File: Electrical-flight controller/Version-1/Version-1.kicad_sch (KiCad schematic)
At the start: 48 parts, among them J1 USB_B_Micro, J2 Conn_01x08_Socket, Q1 S8050, Q2 S8050, Q4 BSS138, SW1 SW_MEC_5G, SW2 SW_MEC_5G, U1 ESP32-WROOM-32, U2 W25Q128JVE, U3 74LS04, U4 CP2102N-Axx-xQFN28, U5 AMS1117, U6 BMP390L, U7 ICM-20948

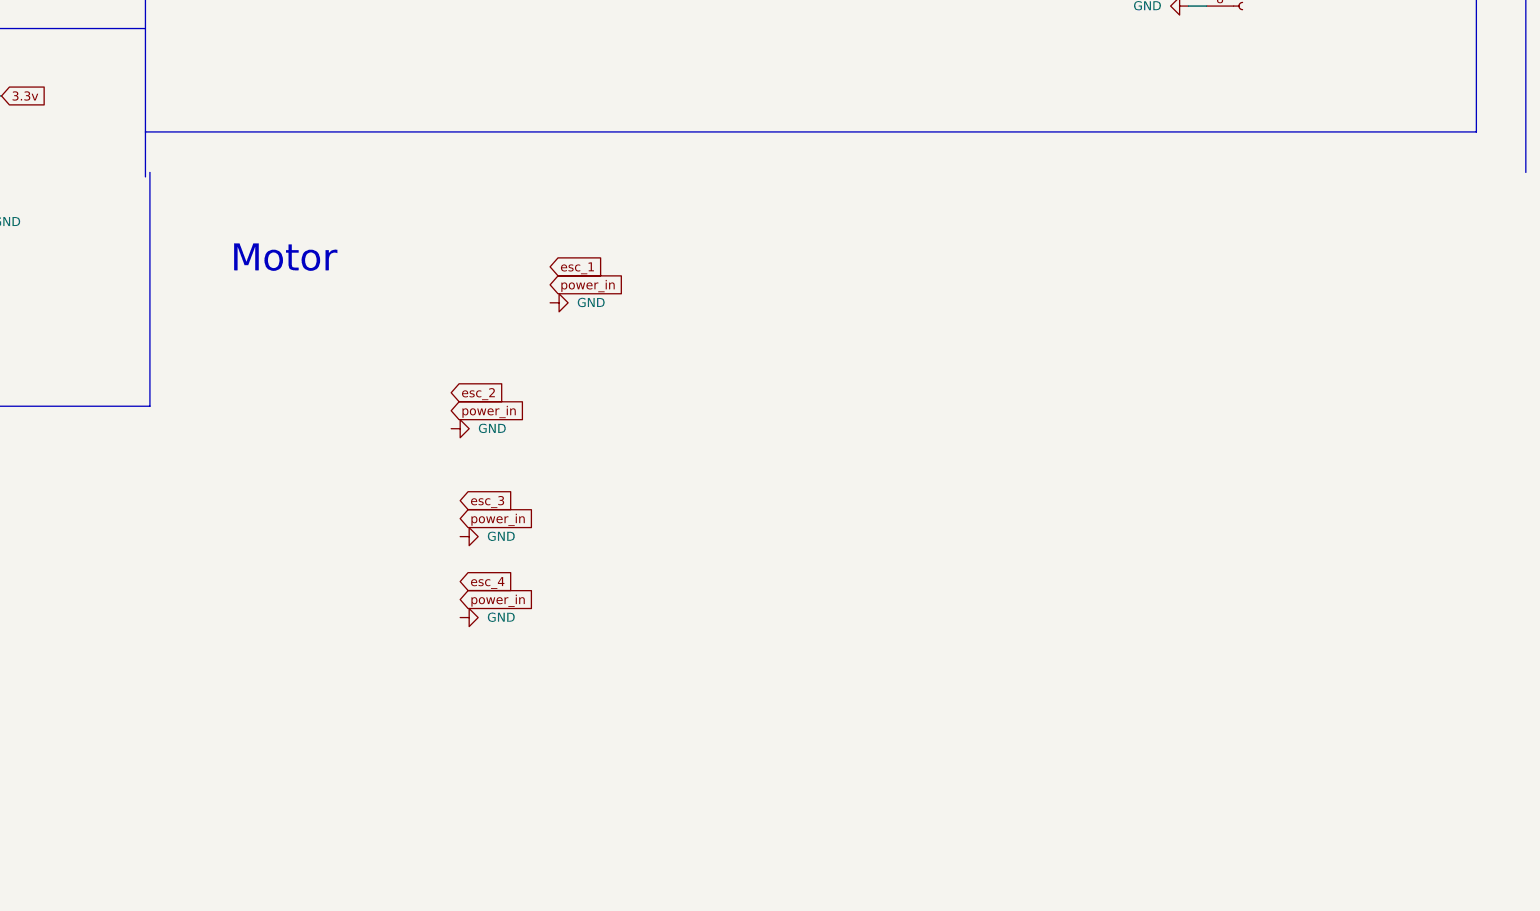
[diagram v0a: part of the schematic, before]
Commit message: added motor drivers
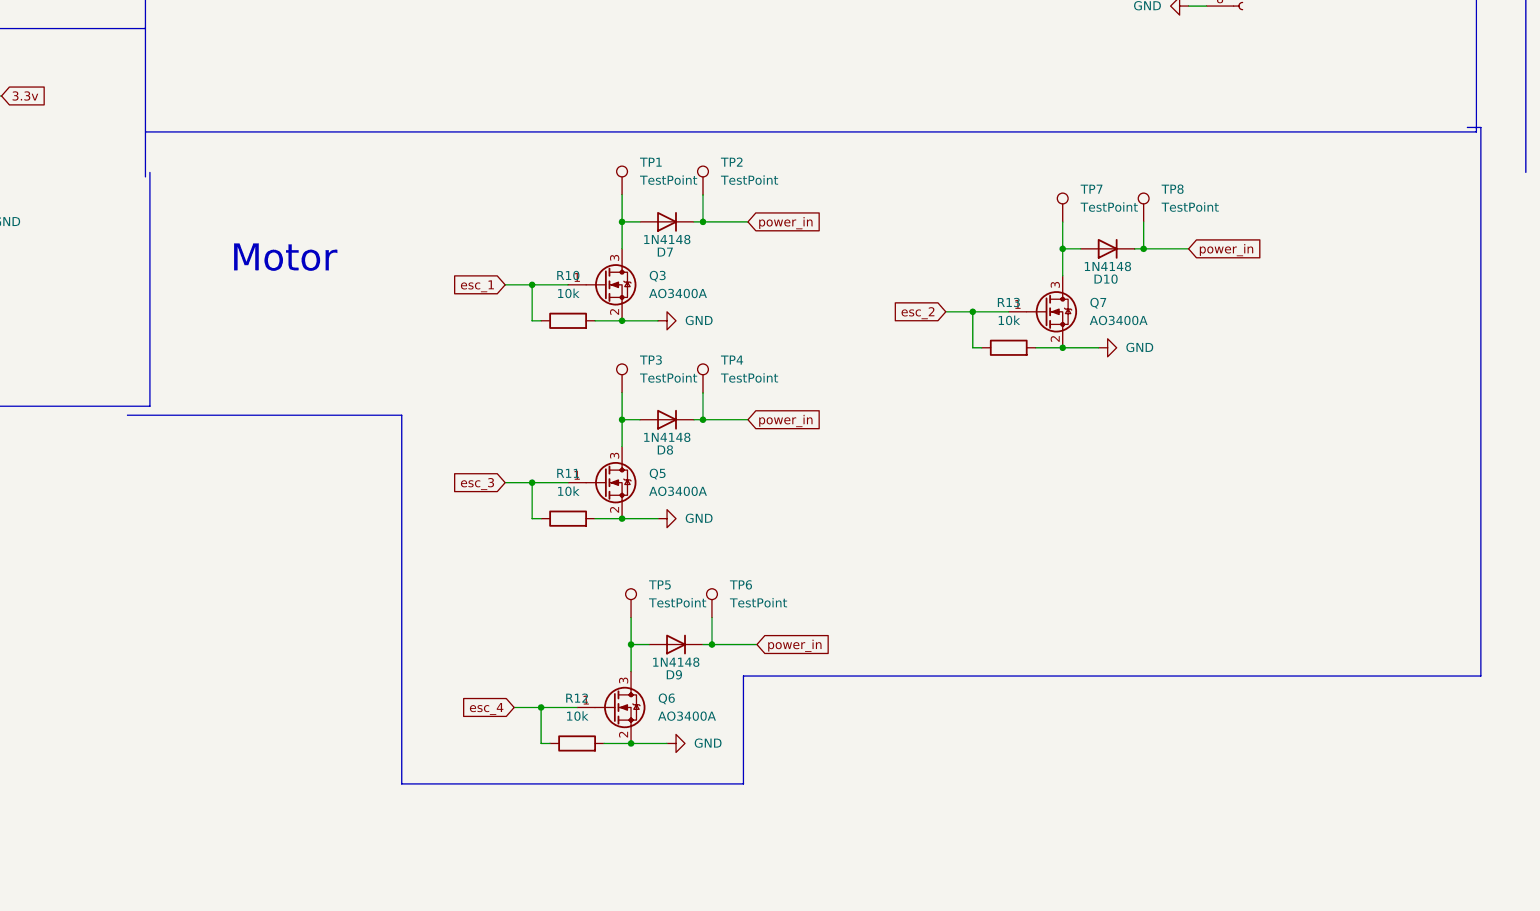
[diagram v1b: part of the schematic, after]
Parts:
- added D10, D7, D8, D9: 1N4148, Diode_THT:D_DO-35_SOD27_P7.62mm_Horizontal, symbol Diode:1N4148
- added Q3, Q5, Q6, Q7: AO3400A, Package_TO_SOT_SMD:SOT-23, symbol Transistor_FET:AO3400A
- added R10, R11, R12, R13: 10k, symbol Device:R
- added TP1, TP2, TP3, TP4, TP5, TP6, TP7, TP8: TestPoint, symbol Connector:TestPoint
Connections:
- net GND: now also Q3.2 (S), Q5.2 (S), Q6.2 (S), Q7.2 (S), R10.2, R11.2, R12.2, R13.2
- net esc_1: now also Q3.1 (G), R10.1
- net esc_2: now also Q7.1 (G), R13.1
- net esc_3: now also Q5.1 (G), R11.1
- net esc_4: now also Q6.1 (G), R12.1
- net power_in: now also D10.1 (K), D7.1 (K), D8.1 (K), D9.1 (K), TP2.1, TP4.1, TP6.1, TP8.1
- new net: D8.2 (A), Q5.3 (D), TP3.1
- new net: D9.2 (A), Q6.3 (D), TP5.1
- new net: D10.2 (A), Q7.3 (D), TP7.1
- new net: D7.2 (A), Q3.3 (D), TP1.1

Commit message: schematic complete!
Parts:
- added C10: 22uF, symbol Device:C
- added C11, C12: C, symbol Device:C
- added C23: 10uF, Capacitor_SMD:C_0603_1608Metric, symbol Device:C
- added C9: 10uF, symbol Device:C
- added D17: PMEG6020ER, Diode_SMD:Nexperia_CFP3_SOD-123W, symbol Diode:PMEG6020ER
- added J3: Conn_01x02_Socket, symbol Connector:Conn_01x02_Socket
- added L1: 1uF, symbol Device:L
- added Q8: DMG2301L, Package_TO_SOT_SMD:SOT-23, symbol Transistor_FET:DMG2301L
- added R17: 732K, symbol Device:R
- added R18: 100K, symbol Device:R
- added U8: TPS61022, Package_DFN_QFN:Texas_RWU0007A_VQFN-7_2x2mm_P0.5mm, symbol Converter_DCDC:TPS61022
- added U9: LTC4412xS6, Package_TO_SOT_SMD:TSOT-23-6, symbol Power_Management:LTC4412xS6
- R10, R11, R12, R13: value 10k -> 10K
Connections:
- net +3.3V: no longer BZ1.1 (+)
- net 3.3v: now also BZ1.1 (+)
- net 5v: now also D17.2 (A); no longer C3.1, R4.1, U5.3 (VI)
- net GND: now also C10.2, C11.2, C12.2, C23.2, C9.2, J3.2 (Pin_2), R18.2, U8.1 (GND), U9.2 (GND), U9.3 (CTL)
- net power_in: no longer D10.1 (K), D7.1 (K), D8.1 (K), D9.1 (K), TP2.1, TP4.1, TP6.1, TP8.1
- new net: R17.2, R18.1, U8.4 (FB)
- new net: Q8.1 (G), U9.5 (GATE)
- new net: L1.2, U8.2 (SW)
- new net BAT+: C9.1, J3.1 (Pin_1), L1.1, U8.5 (EN), U8.7 (VIN)
- new net BAT_IN: C10.1, C11.1, C12.1, D10.1 (K), D7.1 (K), D8.1 (K), D9.1 (K), Q8.3 (D), R17.1, TP2.1, TP4.1, TP6.1, TP8.1, U8.3 (VOUT), U9.1 (VIN)
- new net SWITCHOUT: C23.1, C3.1, D17.1 (K), Q8.2 (S), R4.1, U5.3 (VI), U9.6 (SENSE)
- no-connect marks 32 -> 33

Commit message: imported footprints and assigned them
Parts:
- removed TP1, TP2, TP3, TP4, TP5, TP6, TP7, TP8: TestPoint, symbol Connector:TestPoint
- added J4, J5, J6, J7: Conn_01x02_Socket, Connector_JST:JST_PH_B2B-PH-K_1x02_P2.00mm_Vertical, symbol Connector:Conn_01x02_Socket
- C1, C10, C2, C3, C4, C5, C6, C7, C8, C9: footprint (none) -> Capacitor_SMD:C_0603_1608Metric
- C11, C12: value C -> 22uF; footprint (none) -> Capacitor_SMD:C_0603_1608Metric
- D1: footprint (none) -> LED_SMD:LED_0201_0603Metric
- D2, D3, D4: footprint (none) -> LESD5D5.0CT1G:TVS_LESD5D5.0CT1G
- D6: footprint (none) -> ESD33v88DC:ESD33v88DC
- J1: footprint (none) -> Connector_USB:USB_Micro-B_GCT_USB3076-30-A
- J2: footprint (none) -> Connector_PinSocket_2.54mm:PinSocket_1x08_P2.54mm_Vertical
- J3: footprint (none) -> Connector_JST:JST_PH_B2B-PH-K_1x02_P2.00mm_Vertical
- L1: value 1uF -> 1uH; footprint (none) -> MLF2012A1R0KT000:INDC2012X105N
- R1, R10, R11, R12, R13, R14, R15, R16, R17, R18, R2, R3, R4, R5, R6, R7, R8, R9: footprint (none) -> Resistor_SMD:R_0402_1005Metric
- SW1, SW2: footprint (none) -> TS-1187A-B-A-B:SW_TS-1187A-B-A-B
- U3: footprint (none) -> Package_DIP:DIP-14_W7.62mm_Socket_LongPads
- U6: footprint barometer:XDCR_BMP390L.kicad_mod -> Package_LGA:ST_HLGA-10_2x2mm_P0.5mm_LayoutBorder3x2y
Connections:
- net +3.3V is gone; now on net 3.3v: J2.3 (Pin_3)
- net EP is gone; now on net GND: U2.9 (EP)
- net BAT_IN: now also J4.2 (Pin_2), J5.2 (Pin_2), J6.2 (Pin_2), J7.2 (Pin_2)
- net DI: now also U1.27 (IO16); no longer U1.13 (IO14)
- net DO: now also U1.28 (IO17); no longer U1.27 (IO16)
- net I2C-CL: now also U1.36 (IO22); no longer U1.28 (IO17)
- net IO13: now also U1.16 (IO13)
- net IO15: now also U1.23 (IO15)
- net SCK: no longer U1.16 (IO13), U2.6 (CLK)
- net USB_DN: now also U4.5 (D-)
- net USB_DP: no longer U4.5 (D-)
- net at D8.2 (A), Q5.3 (D): now also J5.1 (Pin_1)
- net at D9.2 (A), Q6.3 (D): now also J6.1 (Pin_1)
- net at D10.2 (A), Q7.3 (D): now also J7.1 (Pin_1)
- net at D7.2 (A), Q3.3 (D): now also J4.1 (Pin_1)
- new net SCK_flash: U1.13 (IO14), U2.6 (CLK)
- no-connect marks 33 -> 41
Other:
- moved on the sheet: C10, C11, C12, C9, J3, L1, R17, R18, U8

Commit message: started pcb -- all basic setups
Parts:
- removed U3: 74LS04, Package_DIP:DIP-14_W7.62mm_Socket_LongPads, symbol 74xx:74LS04
- added CR1, CR2, CR3: 1SS404_H3FT, USC_TOS:USC_TOS, symbol 1SS404:1SS404_H3FT
- U6: footprint Package_LGA:ST_HLGA-10_2x2mm_P0.5mm_LayoutBorder3x2y -> BMP390L:BMP390L; Availability In Stock -> (none); Check_prices https://www.snapeda.com/parts/BMP390L/Bosch/view-part/?ref=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 -> (none); Description_1 Pressure Sensor Development Tools Evaluation Shuttle Board 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 -> (none); MANUFACTURER BOSCH -> (none); MAXIMUM_PACKAGE_HEIGHT 0.8 mm -> (none); MF Bosch Sensortec -> (none); MP BMP390L -> (none); PARTREV 1.7 -> (none); Package None -> (none); Price None -> (none); SNAPEDA_PN BMP390L -> (none); STANDARD Manufacturer Recommendation -> (none); SnapEDA_Link https://www.snapeda.com/parts/BMP390L/Bosch/view-part/?ref=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 -> (none)
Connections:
- net 3.3v: now also CR1.2, CR2.2; no longer U6.5 (SDO/DNC/SA0), U7.9 (SDO/AD0)
- net CTS: now also U4.23 (~{CTS})
- net DTR: now also U4.28 (~{DTR})
- net RTS: now also U4.24 (~{RTS})
- net SWITCHOUT: now also CR3.2; no longer U5.3 (VI)
- net power_in renamed VCC
- new net: CR1.1, U7.9 (SDO/AD0)
- new net: CR3.1, U5.3 (VI)
- new net: CR2.1, U6.5 (SDO)
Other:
- moved on the sheet: C3, D1, R20, R4

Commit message: bt drone_1
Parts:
- removed CR1, CR2, CR3: 1SS404_H3FT, USC_TOS:USC_TOS, symbol 1SS404:1SS404_H3FT
- added CR1, CR2: PESD3V3L1BA_115, DIODE_PESD3V3L1BA_115_NEX, symbol PESD3V3L1BA_115_NEX:PESD3V3L1BA_115
- added D11: LED, LED_SMD:LED_0201_0603Metric, symbol Device:LED
- added D18: PMEG6020ER, Diode_SMD:Nexperia_CFP3_SOD-123W, symbol Diode:PMEG6020ER
- added Q9: DMG2301L, Package_TO_SOT_SMD:SOT-23, symbol Transistor_FET:DMG2301L
- added R25: 470k, symbol Device:R
- added R26: 2K, Resistor_SMD:R_0402_1005Metric, symbol Device:R
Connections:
- net 3.3v: now also CR1.2, CR2.2
- net BAT_IN: no longer D10.1 (K), D7.1 (K), D8.1 (K), D9.1 (K), J4.2 (Pin_2), J5.2 (Pin_2), J6.2 (Pin_2), J7.2 (Pin_2)
- net GND: now also D11.1 (K)
- net SWITCHOUT: now also D18.2 (A), Q9.2 (S), R25.1; no longer D17.1 (K)
- net R9_Q2: now reaches Q2.2 (B), R9.2
- net at U9.4 (STAT): now also Q9.1 (G), R25.2, R26.1
- net at U7.9 (SDO/AD0): now also CR2.1
- net at U5.3 (VI): now also D18.1 (K)
- net R8_Q1: now reaches Q1.2 (B), R8.2
- net at U6.5 (SDO): now also CR1.1
- new net: D11.2 (A), R26.2
- new net: D17.1 (K), Q9.3 (D)
- new net BAT_IN_1: D10.1 (K), D7.1 (K), D8.1 (K), D9.1 (K), J4.2 (Pin_2), J5.2 (Pin_2), J6.2 (Pin_2), J7.2 (Pin_2)
- no-connect marks 41 -> 40
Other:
- moved on the sheet: C23, D1, D17, Q1, Q2
